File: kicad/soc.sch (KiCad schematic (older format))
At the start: 16 parts, among them P1 LED MATRIX, P2 ALTERA_DE1_GPIO, Q1 NPN_CBE, Q2 NPN_CBE, Q3 NPN_CBE, SW1 RGB_rotary_encoder, U1 speakjet

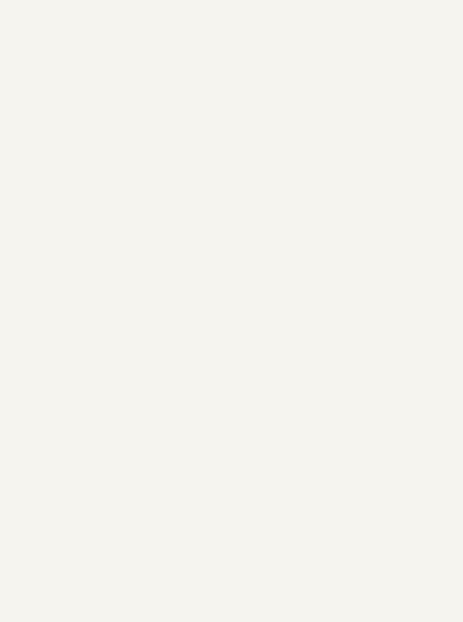
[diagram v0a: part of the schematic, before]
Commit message: some work on schematic incorporating the lcd touchscreen
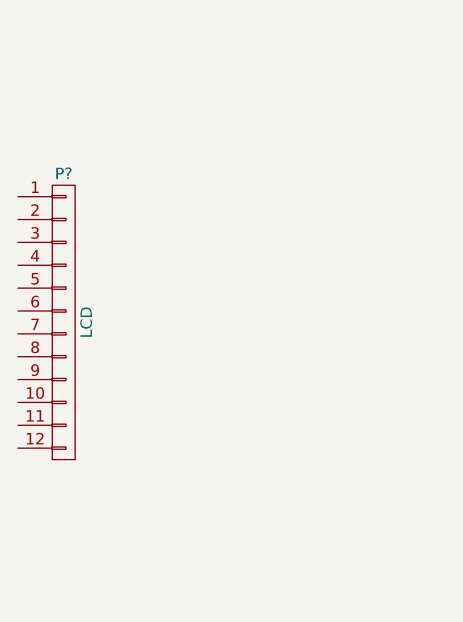
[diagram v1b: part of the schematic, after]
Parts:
- added P?: LCD, symbol CONN_01X12
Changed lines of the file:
@@
 Text Label 6250 3700 2    60   ~ 0
 ~OE
+$Comp
+L CONN_01X12 P?
+U 1 1 55A2C271
+P 3900 2500
+F 0 "P?" H 3900 3150 50  0000 C CNN
+F 1 "LCD" V 4000 2500 50  0000 C CNN
+F 2 "" H 3900 2500 60  0000 C CNN
+F 3 "" H 3900 2500 60  0000 C CNN
+	1    3900 2500
+	1    0    0    -1
+$EndComp
 $EndSCHEMATC

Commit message: some work on support board
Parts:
- removed P?: LCD, symbol CONN_01X12
- removed Q1, Q2, Q3: NPN_CBE, symbol NPN_CBE
- removed R1, R2, R3: 1K, symbol R
- removed R4, R5, R6: 330, symbol R
- removed R7, R8, R9: 10K, symbol R
- removed SW1: RGB_rotary_encoder, symbol RGB_rotary_encoder
- added P3: RTC header, Socket_Strips:Socket_Strip_Straight_1x07, symbol CONN_01X07
- added P4: PS/2 Keyboard, symbol CONN_01X06
- added P5: PS/2 mouse, symbol CONN_01X06
- P1: footprint (none) -> Pin_Headers:Pin_Header_Straight_2x08
- P2: footprint (none) -> mstock:PIN_ARRAY_20X2_LARGE
- U1: footprint (none) -> Housings_DIP:DIP-18_W7.62mm
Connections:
- net +3V3: now also P3.2 (P2)
- net +5V: now also P4.4 (P4)
- net GND: now also P3.1 (P1), P4.3 (P3), P5.3 (P3)
- net ROTARY_B: no longer names the net of P2.21 (IO_A18)
- net ROTARY_CW: no longer names the net of P2.19 (IO_A16)
- net ROTARY_CW: no longer P2.20 (IO_A17)
- net ROTARY_G: no longer names the net of P2.22 (IO_A19)
- net ROTARY_R: no longer names the net of P2.23 (IO_A20)
- net ROTARY_SW: no longer names the net of P2.18 (IO_A15)
- new net KBD_CLK: P4.5 (P5)
- new net KBD_DATA: P4.1 (P1)
- new net MISO_33: P3.5 (P5)
- new net MOSI_33: P3.6 (P6)
- new net MOUSE_CLK: P5.5 (P5)
- new net MOUSE_DATA: P5.1 (P1)
- new net SCLK_33: P3.4 (P4)
- new net ~RTC_SS: P3.7 (P7)
- no-connect marks 4 -> 9

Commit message: some kicad stuff
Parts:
- removed P4: PS/2 Keyboard, symbol CONN_01X06
- removed P5: PS/2 mouse, symbol CONN_01X06
- added C1: .001uF, Capacitors_SMD:C_0603_HandSoldering, symbol C
- added J1: JACK_TRS_3PINS, mstock-pretty:SJI-3513N, symbol JACK_TRS_3PINS
- added J2: PS/2 Keyboard, mstock-pretty:MD-60S, symbol Mini_DIN-6
- added J3: PS/2 Mouse, mstock-pretty:MD-60S, symbol Mini_DIN-6
- added P10: CODEC right, Socket_Strips:Socket_Strip_Straight_1x16, symbol CONN_01X16
- added P11: CODEC inputs, Pin_Headers:Pin_Header_Straight_1x04, symbol CONN_01X04
- added P6: Amp in, Socket_Strips:Socket_Strip_Straight_1x02, symbol CONN_01X02
- added P7: Amp pwr, Socket_Strips:Socket_Strip_Straight_1x03, symbol CONN_01X03
- added P8: Amp out, Socket_Strips:Socket_Strip_Straight_1x02, symbol CONN_01X02
- added P9: CODEC left, Socket_Strips:Socket_Strip_Straight_1x16, symbol CONN_01X16
- added R1, R2, R3: 10k, Resistors_SMD:R_0603_HandSoldering, symbol R
- added SP1: SPEAKER, Pin_Headers:Pin_Header_Angled_1x02, symbol SPEAKER
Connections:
- net labels added: CODEC_DIRQ, CODEC_MISO, CODEC_MOSI, CODEC_SCLK, Kbd_clk, Kbd_data, Mouse_clk, Mouse_data, ~CODEC_CS, ~CODEC_XDCS, ~RST
- net labels removed: KBD_CLK, KBD_DATA, MOUSE_CLK, MOUSE_DATA
- wire segments 36 -> 78
- no-connect marks 9 -> 11

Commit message: some rework of support board, using the CODEC carrier board, the RTC, and headphone, PS/2 jacks
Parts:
- removed C1: .001uF, Capacitors_SMD:C_0603_HandSoldering, symbol C
- removed P3: RTC header, Socket_Strips:Socket_Strip_Straight_1x07, symbol CONN_01X07
- removed P6: Amp in, Socket_Strips:Socket_Strip_Straight_1x02, symbol CONN_01X02
- removed P7: Amp pwr, Socket_Strips:Socket_Strip_Straight_1x03, symbol CONN_01X03
- removed P8: Amp out, Socket_Strips:Socket_Strip_Straight_1x02, symbol CONN_01X02
- removed R1, R2, R3: 10k, Resistors_SMD:R_0603_HandSoldering, symbol R
- removed SP1: SPEAKER, Pin_Headers:Pin_Header_Angled_1x02, symbol SPEAKER
- removed U1: speakjet, Housings_DIP:DIP-18_W7.62mm, symbol speakjet
- added BT1: 2025 coin cell, mstock-pretty:coincell, symbol Battery
- added U2: DS3234, Housings_SOIC:SOIC-20_7.5x12.8mm_Pitch1.27mm, symbol DS3234
- P2: footprint mstock:PIN_ARRAY_20X2_LARGE -> Pin_Headers:Pin_Header_Straight_2x20
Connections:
- wire segments 78 -> 46
- no-connect marks 11 -> 9

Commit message: close to final
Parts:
- removed P11: CODEC inputs, Pin_Headers:Pin_Header_Straight_1x04, symbol CONN_01X04
- added C1, C2: 10nF, Capacitors_SMD:C_0805_HandSoldering, symbol C
- added C3, C4: 1uF, Capacitors_SMD:C_0805_HandSoldering, symbol C
- added J4: Line In, mstock-pretty:SJI-3513N, symbol JACK_TRS_3PINS
- added P3: Bluetooth, Socket_Strips:Socket_Strip_Straight_1x09, symbol CONN_01X09
- added P4: CONN_01X08, Pin_Headers:Pin_Header_Straight_2x04, symbol CONN_01X08
- added R1, R2: 470, Resistors_SMD:R_0805_HandSoldering, symbol R
- J1: value JACK_TRS_3PINS -> Line Out
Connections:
- net +3V3: now also P4.7 (P7)
- net +5V: now also P3.9 (P9)
- net GND: now also P3.8 (P8), P4.8 (P8)
- net MISO_33: now also P3.2 (P2)
- net MOSI_33: now also P3.3 (P3)
- net SCLK_33: now also P3.1 (P1)
- net ~RST: now also P3.7 (P7)
- net IO_17: now reaches P2.20 (IO_A17)
- net IO_17: now also P4.1 (P1)
- net ~BLE_CS: now reaches P2.21 (IO_A18)
- net ~BLE_CS: now also P3.4 (P4)
- net IO_19: now reaches P2.22 (IO_A19)
- net IO_19: now also P4.2 (P2)
- net IO_20: now reaches P2.23 (IO_A20)
- net IO_20: now also P4.3 (P3)
- net BLE_IRQ: now reaches P2.24 (IO_A21)
- net BLE_IRQ: now also P3.5 (P5)
- net IO_30: now reaches P2.35 (IO_A30)
- net IO_30: now also P4.4 (P4)
- net IO_31: now reaches P2.36 (IO_A31)
- net IO_31: now also P4.5 (P5)
- net IO_32: now reaches P2.37 (IO_A32)
- net IO_32: now also P4.6 (P6)
- net GNDA: now reaches J1.1 (S), P9.13 (P13), P9.14 (P14)
- net GNDA: now also P10.13 (P13), C1.2, C2.2, J4.1 (S)
- net L_OUT: now reaches J1.2 (T), P9.15 (P15)
- net R_OUT: now reaches J1.3 (R), P9.16 (P16)
- net L_IN: now reaches P10.15 (P15)
- net L_IN: now also C2.1, R2.2
- net R_IN: now reaches P10.16 (P16)
- net R_IN: now also C1.1, R1.2
- new net: C4.2, J4.2 (T)
- new net: C3.2, J4.3 (R)
- new net: C3.1, R1.1
- new net: C4.1, R2.1
- new net BLE_DEV: P3.6 (P6)
- no-connect marks 9 -> 21
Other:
- moved on the sheet: J1

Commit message: Revert "close to final"
This reverts commit c876cf625f705db1e319b0381db18ed40929d998.
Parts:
- removed C1, C2: 10nF, Capacitors_SMD:C_0805_HandSoldering, symbol C
- removed C3, C4: 1uF, Capacitors_SMD:C_0805_HandSoldering, symbol C
- removed J4: Line In, mstock-pretty:SJI-3513N, symbol JACK_TRS_3PINS
- removed P3: Bluetooth, Socket_Strips:Socket_Strip_Straight_1x09, symbol CONN_01X09
- removed P4: CONN_01X08, Pin_Headers:Pin_Header_Straight_2x04, symbol CONN_01X08
- removed R1, R2: 470, Resistors_SMD:R_0805_HandSoldering, symbol R
- added P11: CODEC inputs, Pin_Headers:Pin_Header_Straight_1x04, symbol CONN_01X04
- J1: value Line Out -> JACK_TRS_3PINS
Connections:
- net at P10.14 (P14): now also P11.3 (P3)
- net BLE_IRQ: no longer names the net of P2.24 (IO_A21)
- net GNDA: no longer names the net of J1.1 (S), P9.13 (P13), P9.14 (P14)
- net GNDA: no longer P10.13 (P13)
- net IO_17: no longer names the net of P2.20 (IO_A17)
- net IO_19: no longer names the net of P2.22 (IO_A19)
- net IO_20: no longer names the net of P2.23 (IO_A20)
- net IO_30: no longer names the net of P2.35 (IO_A30)
- net IO_31: no longer names the net of P2.36 (IO_A31)
- net IO_32: no longer names the net of P2.37 (IO_A32)
- net L_IN: no longer names the net of P10.15 (P15)
- net L_IN: now also P11.2 (P2)
- net L_OUT: no longer names the net of J1.2 (T), P9.15 (P15)
- net R_IN: no longer names the net of P10.16 (P16)
- net R_IN: now also P11.1 (P1)
- net R_OUT: no longer names the net of J1.3 (R), P9.16 (P16)
- net ~BLE_CS: no longer names the net of P2.21 (IO_A18)
- new net: P10.13 (P13), P11.4 (P4)
- no-connect marks 21 -> 9
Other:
- moved on the sheet: J1
